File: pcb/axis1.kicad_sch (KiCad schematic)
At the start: 10 parts, among them J11 Mini v1.0 FEMALE sockets, J21 MOTOR PHASES male 1x3, J31 ENCODER JST-SH 6p, J41 MINI POWER: +12V / GND

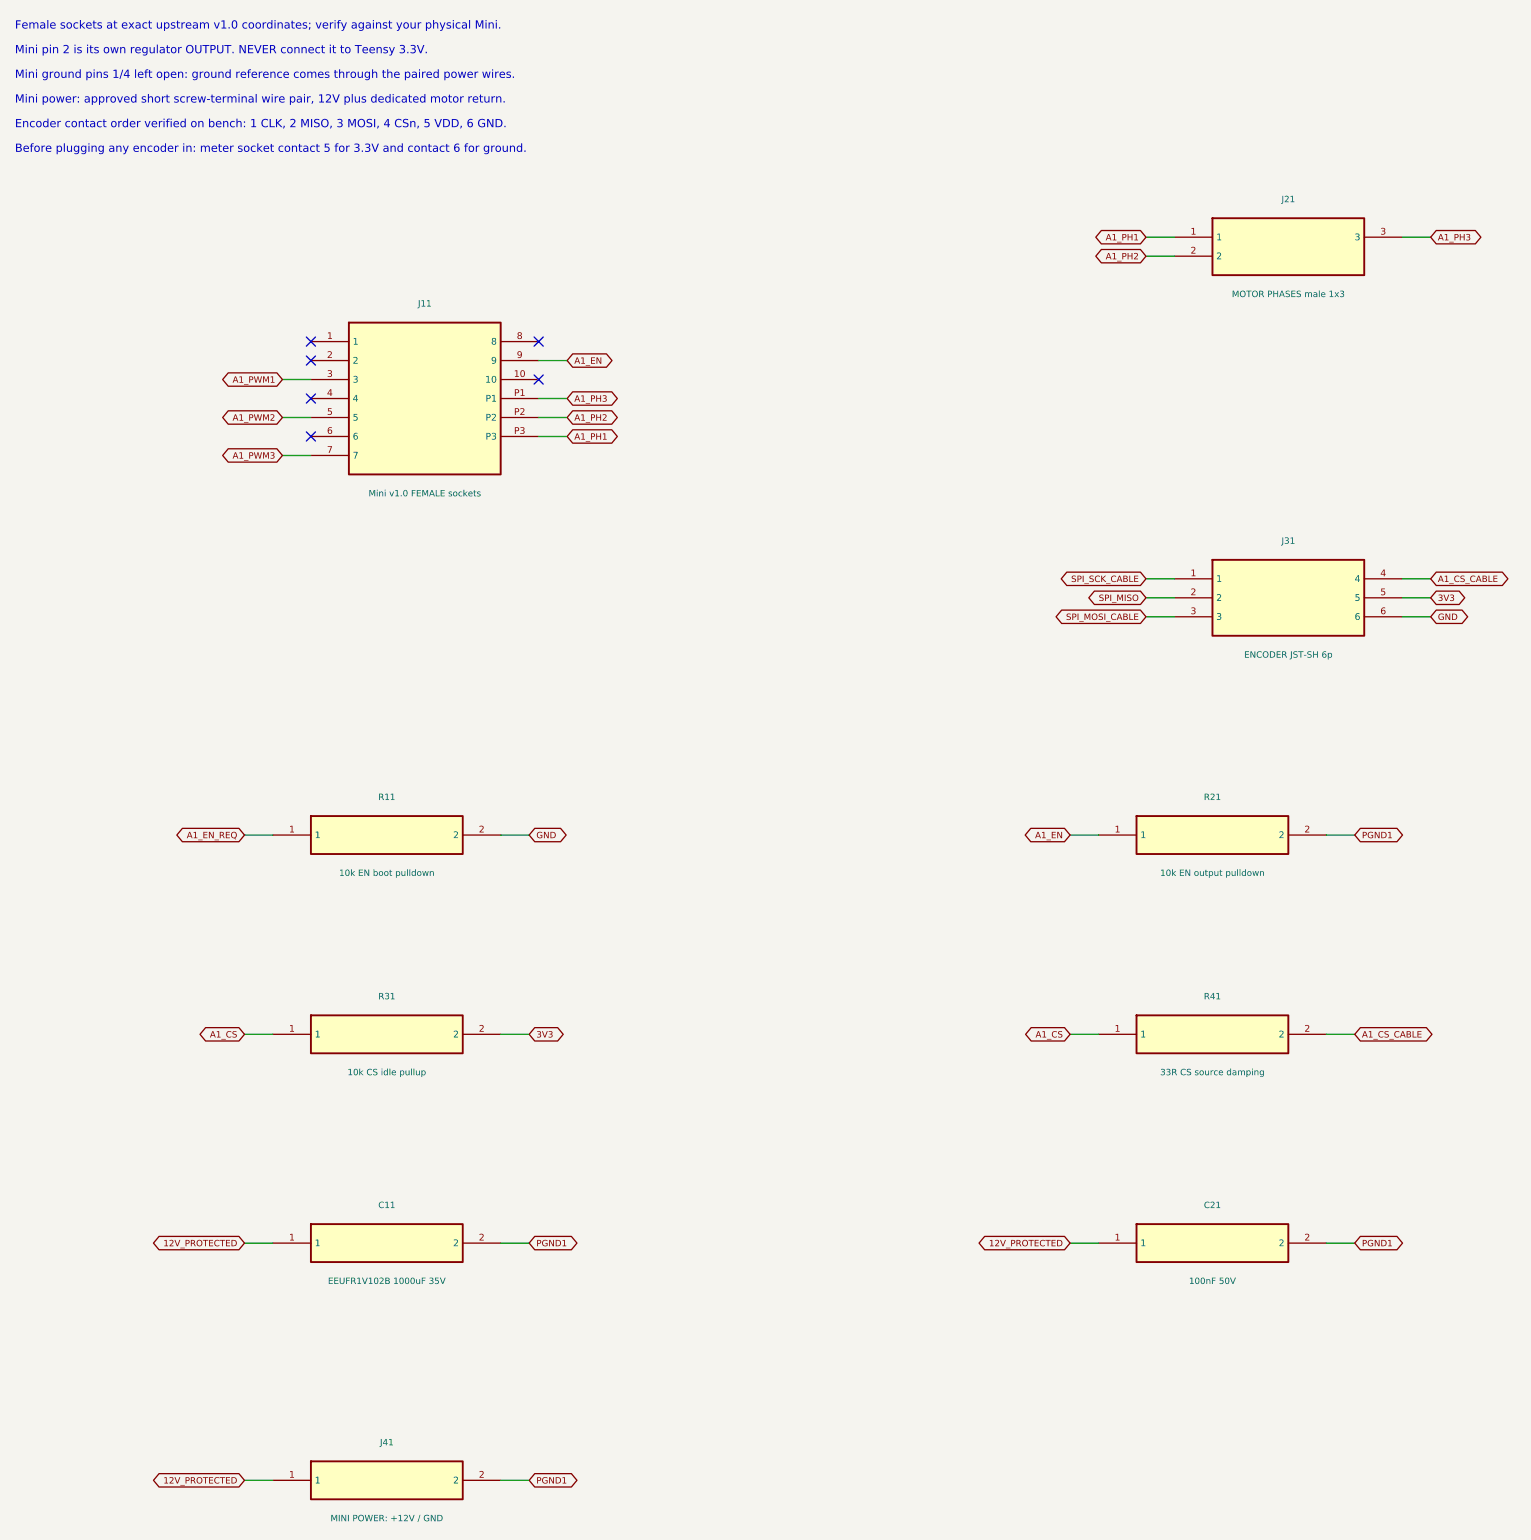
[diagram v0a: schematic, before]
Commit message: feat: finish through-hole six-axis carrier review design
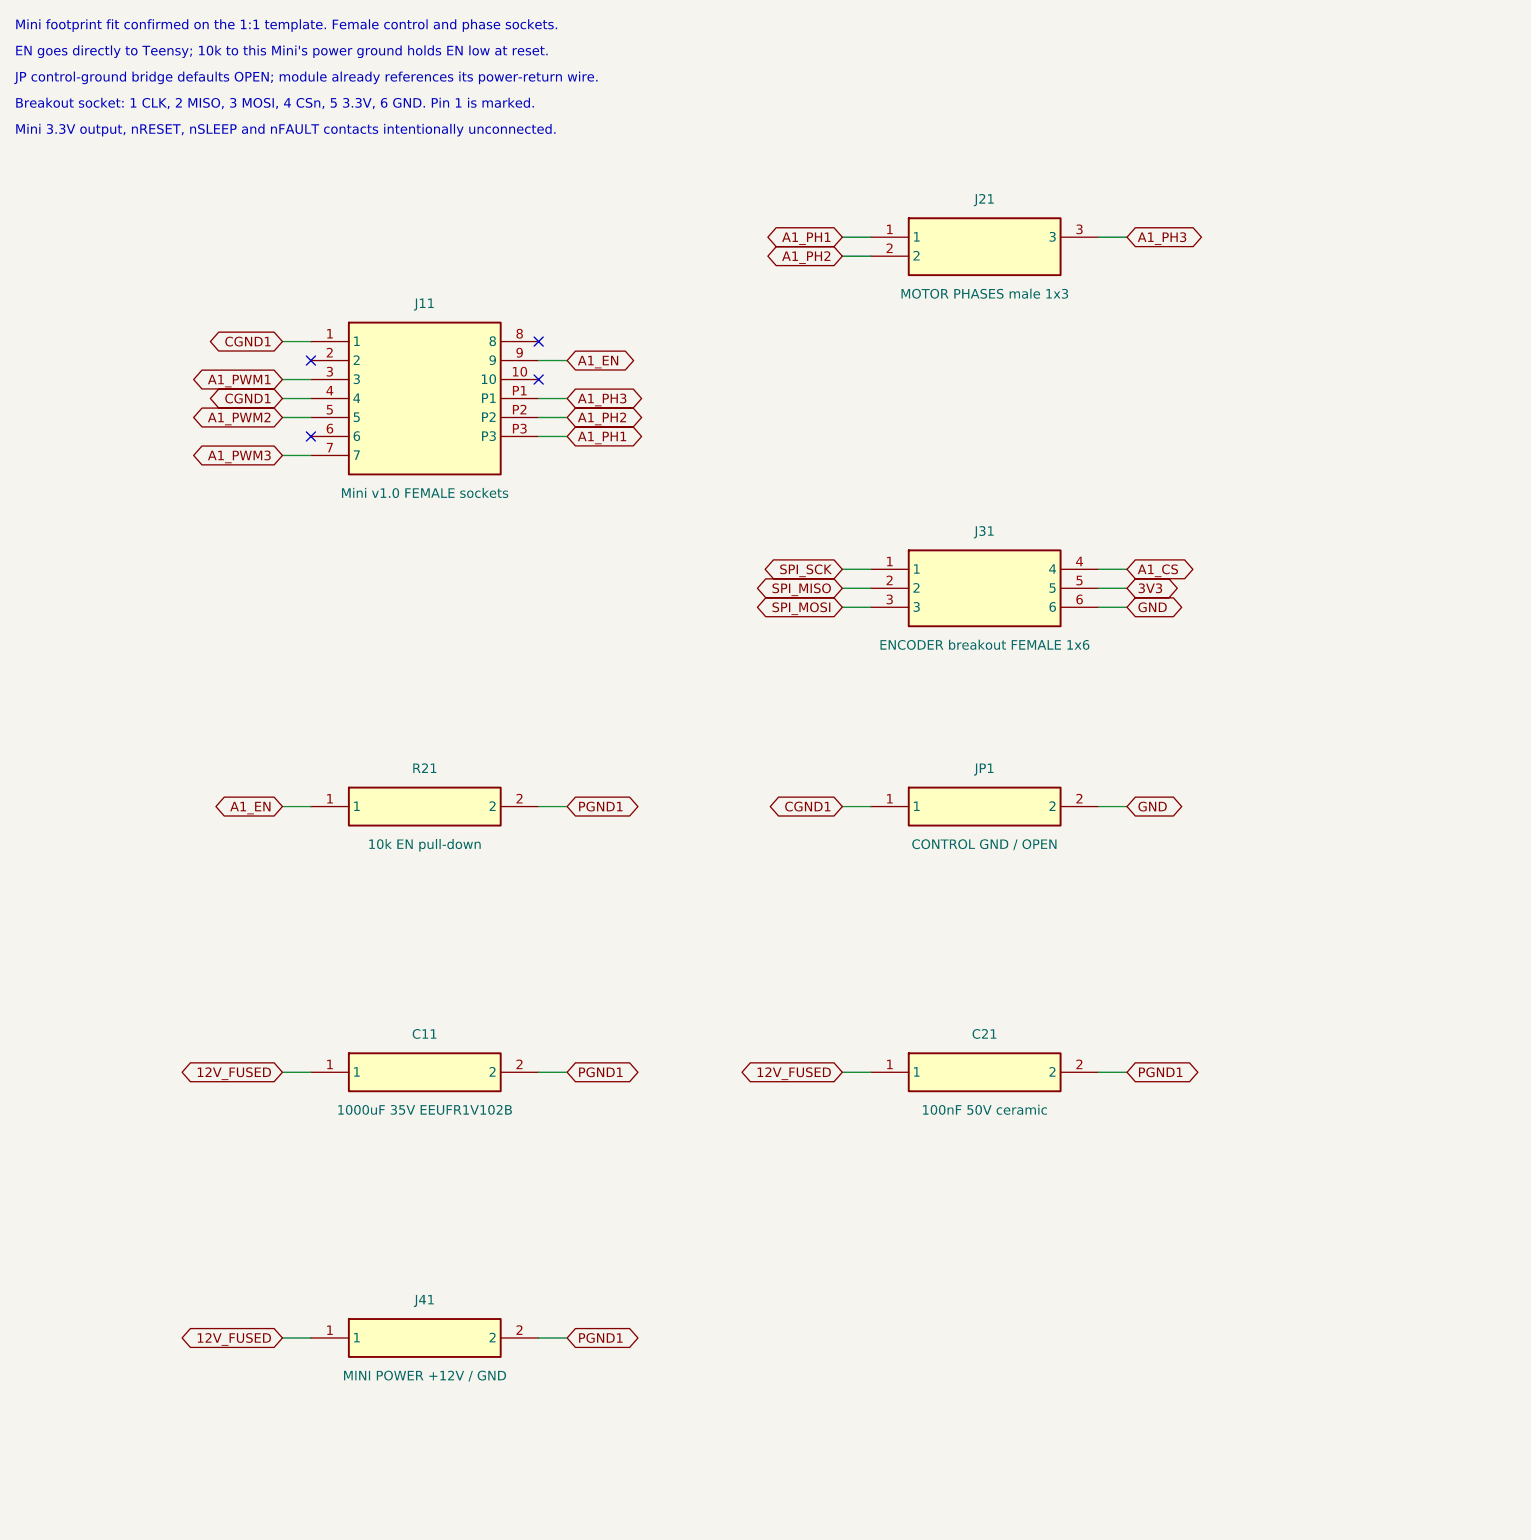
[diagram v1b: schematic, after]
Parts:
- removed R11: 10k EN boot pulldown, Resistor_SMD:R_0603_1608Metric, symbol TrueSkate:R11
- removed R31: 10k CS idle pullup, Resistor_SMD:R_0603_1608Metric, symbol TrueSkate:R31
- removed R41: 33R CS source damping, Resistor_SMD:R_0603_1608Metric, symbol TrueSkate:R41
- added JP1: CONTROL GND / OPEN, TrueSkate:GroundBridge_THT, symbol TrueSkate:JP1
- C11: value EEUFR1V102B 1000uF 35V -> 1000uF 35V EEUFR1V102B; LCSC C128476 -> (none)
- C21: value 100nF 50V -> 100nF 50V ceramic; footprint Capacitor_SMD:C_0603_1608Metric -> Capacitor_THT:C_Disc_D5.0mm_W2.5mm_P5.00mm; LCSC C14663 -> (none)
- J31: value ENCODER JST-SH 6p -> ENCODER breakout FEMALE 1x6; footprint Connector_JST:JST_SH_BM06B-SRSS-TB_1x06-1MP_P1.00mm_Vertical -> Connector_PinSocket_2.54mm:PinSocket_1x06_P2.54mm_Vertical; LCSC C160392 -> (none)
- J41: value MINI POWER: +12V / GND -> MINI POWER +12V / GND
- R21: value 10k EN output pulldown -> 10k EN pull-down; footprint Resistor_SMD:R_0603_1608Metric -> Resistor_THT:R_Axial_DIN0207_L6.3mm_D2.5mm_P7.62mm_Horizontal; LCSC C25804 -> (none)
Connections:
- net A1_CS_CABLE is gone; now on net A1_CS: J31.4
- net GND: now also JP1.2
- net CGND1: now reaches J11.1
- net CGND1: now also J11.4, JP1.1
- net 12V_PROTECTED renamed 12V_FUSED
- net SPI_MOSI_CABLE renamed SPI_MOSI
- net SPI_SCK_CABLE renamed SPI_SCK
- no-connect marks 6 -> 4
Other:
- note added: "Breakout socket: 1 CLK, 2 MISO, 3 MOSI, 4 CSn, 5 3.3V, 6 GND. Pin 1 is marked."
- note added: "EN goes directly to Teensy; 10k to this Mini's power ground holds EN low at reset."
- note added: "JP control-ground bridge defaults OPEN; module already references its power-return wire."
- note added: "Mini 3.3V output, nRESET, nSLEEP and nFAULT contacts intentionally unconnected."
- note added: "Mini footprint fit confirmed on the 1:1 template. Female control and phase sockets."
- note removed: "Before plugging any encoder in: meter socket contact 5 for 3.3V and contact 6 for ground."
- note removed: "Encoder contact order verified on bench: 1 CLK, 2 MISO, 3 MOSI, 4 CSn, 5 VDD, 6 GND."
- note removed: "Female sockets at exact upstream v1.0 coordinates; verify against your physical Mini."
- note removed: "Mini ground pins 1/4 left open: ground reference comes through the paired power wires."
- note removed: "Mini pin 2 is its own regulator OUTPUT. NEVER connect it to Teensy 3.3V."
- note removed: "Mini power: approved short screw-terminal wire pair, 12V plus dedicated motor return."
- title: 03 / Axis 1: index_curl_1 -> 02 / A1: index_curl_1
- moved on the sheet: C11, C21, J21, J31, J41, R21

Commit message: feat: use exact Mini v1.0 footprints with direct power routing
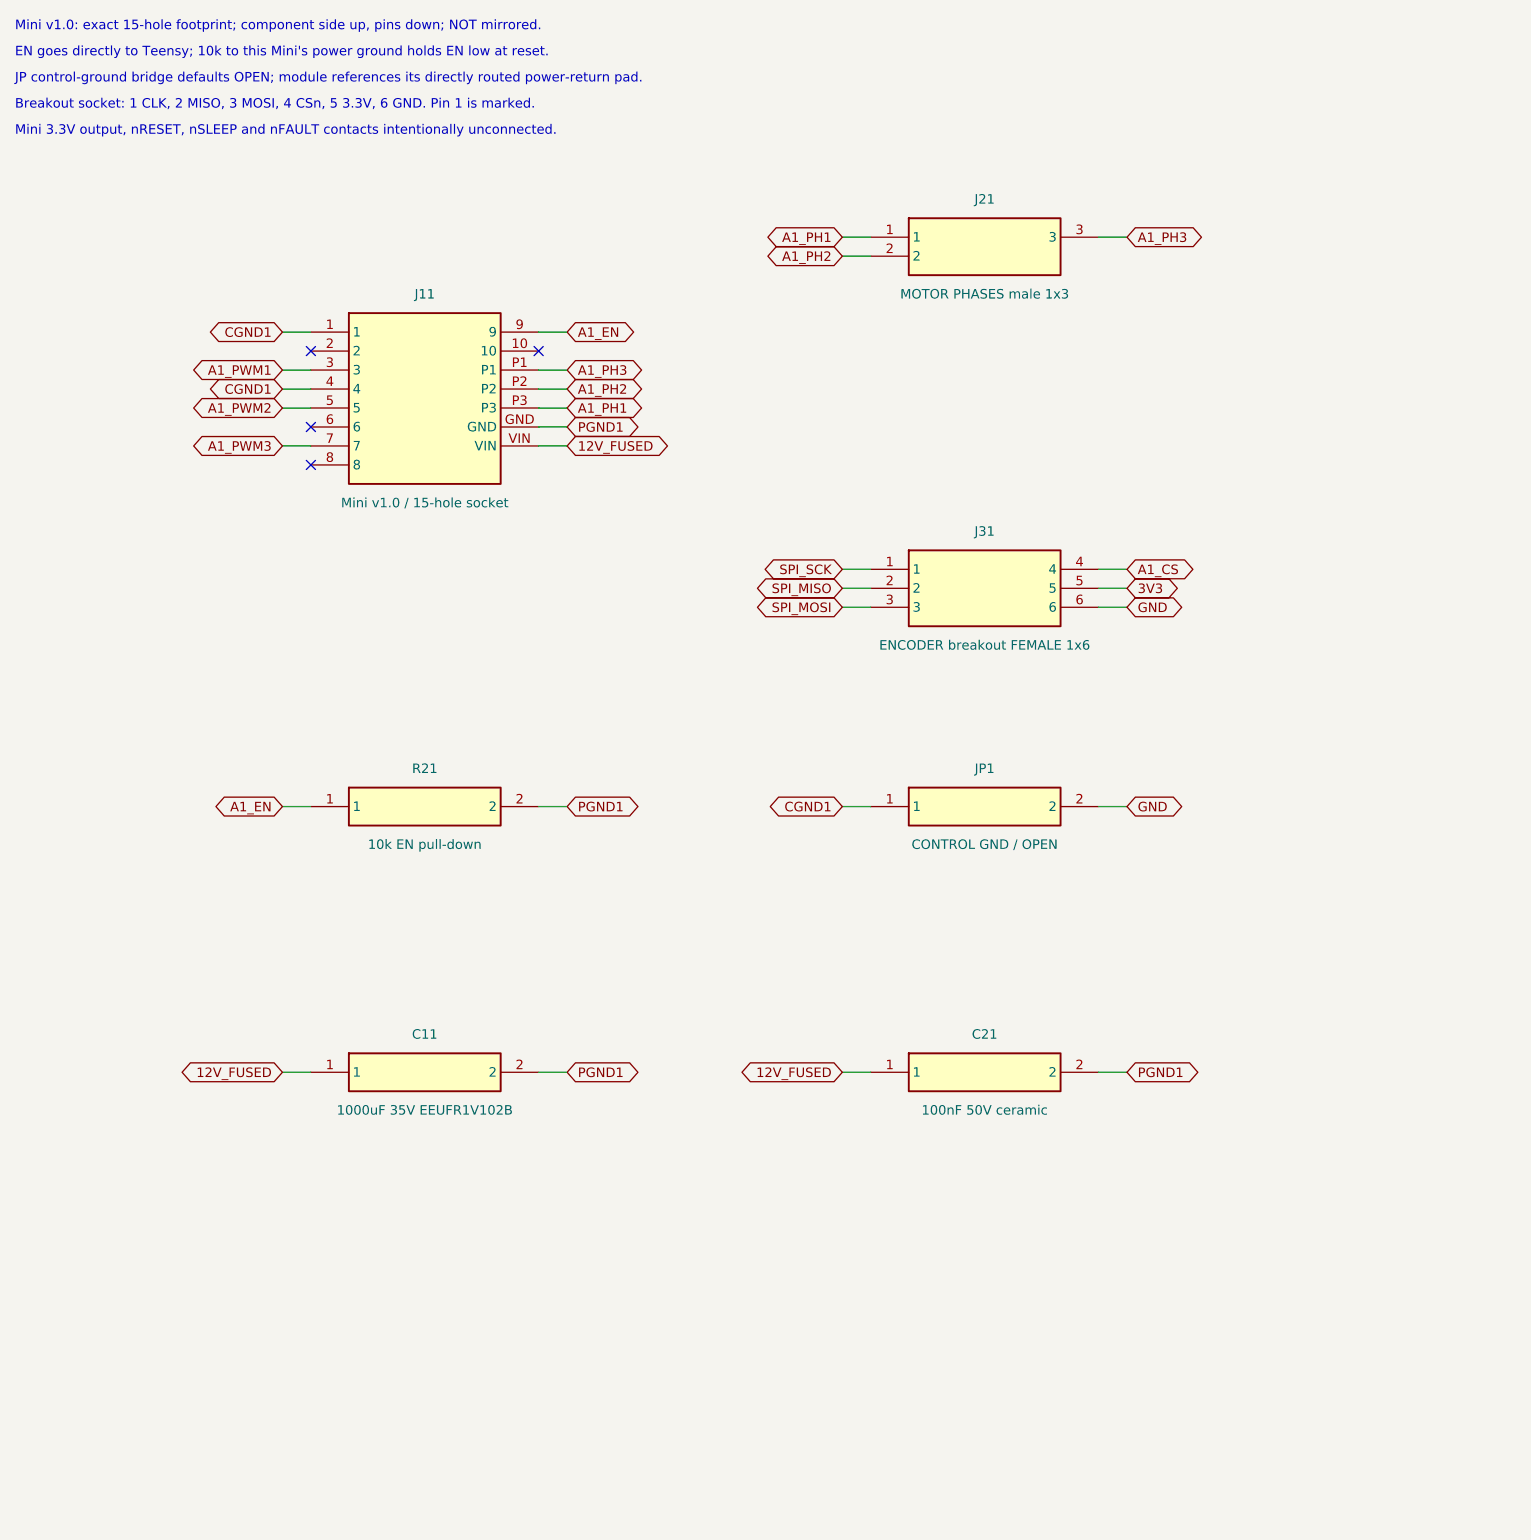
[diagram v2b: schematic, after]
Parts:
- removed J41: MINI POWER +12V / GND, TerminalBlock_Phoenix:TerminalBlock_Phoenix_MKDS-1-2-3.81_1x02_P3.81mm_Horizontal, symbol TrueSkate:J41
- J11: value Mini v1.0 FEMALE sockets -> Mini v1.0 / 15-hole socket; footprint TrueSkate:Mini_v1_Sockets -> TrueSkate:SimpleFOC_Mini_v1.0
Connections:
- net 12V_FUSED: now also J11.VIN
- net PGND1: now also J11.GND
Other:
- note added: "JP control-ground bridge defaults OPEN; module references its directly routed power-return pad."
- note added: "Mini v1.0: exact 15-hole footprint; component side up, pins down; NOT mirrored."
- note removed: "JP control-ground bridge defaults OPEN; module already references its power-return wire."
- note removed: "Mini footprint fit confirmed on the 1:1 template. Female control and phase sockets."
